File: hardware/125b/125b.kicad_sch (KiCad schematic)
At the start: 51 parts, among them J1 Guitar in, J2 Barrel_Jack, J3 Conn_02x05_Odd_Even_MountingP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, J4 Guitar out, SW1 SW_DIP_x02, SW2 RotaryEncoder_Switch, SW3 Switch 1, SW4 Switch 2, U1 L78L05_TO92, U2 TL074

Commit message: Everything connected together
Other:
- moved on the sheet: D1
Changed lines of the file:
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@@
 	(wire
 		(pts
-			(xy 26.67 153.67) (xy 30.48 153.67)
+			(xy 29.21 153.67) (xy 33.02 153.67)
 		)
 		(stroke
@@
 	(wire
 		(pts
+			(xy 19.05 153.67) (xy 21.59 153.67)
+		)
+		(stroke
+			(width 0)
+			(type default)
+		)
+	)
+	(wire
+		(pts
 			(xy 133.35 52.07) (xy 148.59 52.07)
 		)
@@
 	)
 	(label "fsw2"
-		(at 30.48 153.67 0)
+		(at 33.02 153.67 0)
 		(effects
 			(font
@@
 		)
 	)
+	(netclass_flag ""
+		(length 2.54)
+		(shape round)
+		(at 53.34 161.29 0)
+		(fields_autoplaced yes)
+		(effects
+			(font
+				(size 1.27 1.27)
+			)
+			(justify left bottom)
+		)
+		(property "Netclass" "Power"
+			(at 54.0385 158.75 0)
+			(effects
+				(font
+					(size 1.27 1.27)
+				)
+				(justify left)
+			)
+		)
+		(property "Component Class" ""
+			(at 1.27 1.27 0)
+			(effects
+				(font
+					(size 1.27 1.27)
+					(italic yes)
+				)
+			)
+		)
+	)
+	(netclass_flag ""
+		(length 2.54)
+		(shape round)
+		(at 111.76 161.29 0)
+		(fields_autoplaced yes)
+		(effects
+			(font
+				(size 1.27 1.27)
+			)
+			(justify left bottom)
+		)
+		(property "Netclass" "Power"
+			(at 112.4585 158.75 0)
+			(effects
+				(font
+					(size 1.27 1.27)
+				)
+				(justify left)
+			)
+		)
+		(property "Component Class" ""
+			(at -1.27 0 0)
+			(effects
+				(font
+					(size 1.27 1.27)
+					(italic yes)
+				)
+			)
+		)
+	)
+	(netclass_flag ""
+		(length 2.54)
+		(shape round)
+		(at 31.75 153.67 0)
+		(fields_autoplaced yes)
+		(effects
+			(font
+				(size 1.27 1.27)
+			)
+			(justify left bottom)
+		)
+		(property "Netclass" "Power"
+			(at 32.4485 151.13 0)
+			(effects
+				(font
+					(size 1.27 1.27)
+				)
+				(justify left)
+			)
+		)
+		(property "Component Class" ""
+			(at -45.72 8.89 0)
+			(effects
+				(font
+					(size 1.27 1.27)
+					(italic yes)
+				)
+			)
+		)
+	)
+	(netclass_flag ""
+		(length 2.54)
+		(shape round)
+		(at 20.32 153.67 0)
+		(fields_autoplaced yes)
+		(effects
+			(font
+				(size 1.27 1.27)
+			)
+			(justify left bottom)
+		)
+		(property "Netclass" "Power"
+			(at 21.0185 151.13 0)
+			(effects
+				(font
+					(size 1.27 1.27)
+				)
+				(justify left)
+			)
+		)
+		(property "Component Class" ""
+			(at -57.15 8.89 0)
+			(effects
+				(font
+					(size 1.27 1.27)
+					(italic yes)
+				)
+			)
+		)
+	)
+	(netclass_flag ""
+		(length 2.54)
+		(shape round)
+		(at 27.94 161.29 0)
+		(fields_autoplaced yes)
+		(effects
+			(font
+				(size 1.27 1.27)
+			)
+			(justify left bottom)
+		)
+		(property "Netclass" "Power"
+			(at 28.6385 158.75 0)
+			(effects
+				(font
+					(size 1.27 1.27)
+				)
+				(justify left)
+			)
+		)
+		(property "Component Class" ""
+			(at -168.91 17.78 0)
+			(effects
+				(font
+					(size 1.27 1.27)
+					(italic yes)
+				)
+			)
+		)
+	)
 	(symbol
 		(lib_name "GND_15")
@@
 	(symbol
 		(lib_id "Device:LED")
-		(at 22.86 153.67 180)
+		(at 25.4 153.67 180)
 		(unit 1)
 		(exclude_from_sim no)
@@
 		(on_board yes)
 		(dnp no)
-		(fields_autoplaced yes)
 		(property "Reference" "D1"
-			(at 24.4475 146.05 0)
+			(at 29.5275 146.05 0)
 			(effects
 				(font
@@
 		)
 		(property "Value" "LED"
-			(at 24.4475 148.59 0)
+			(at 29.5275 148.59 0)
 			(effects
 				(font
@@
 		)
 		(property "Footprint" "LED_THT:LED_D1.8mm_W3.3mm_H2.4mm"
-			(at 22.86 153.67 0)
+			(at 25.4 153.67 0)
 			(effects
 				(font
@@
 		)
 		(property "Datasheet" "~"
-			(at 22.86 153.67 0)
+			(at 25.4 153.67 0)
 			(effects
 				(font
@@
 		)
 		(property "Description" "Light emitting diode"
-			(at 22.86 153.67 0)
+			(at 25.4 153.67 0)
 			(effects
 				(font
@@
 		)
 		(property "Sim.Pins" "1=K 2=A"
-			(at 22.86 153.67 0)
+			(at 25.4 153.67 0)
 			(effects
 				(font

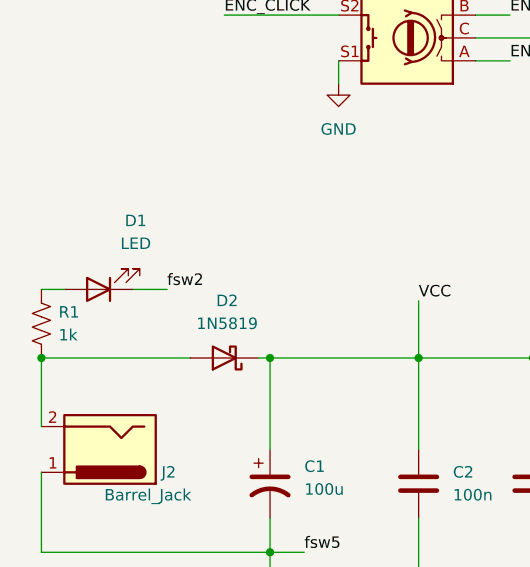
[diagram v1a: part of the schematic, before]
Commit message: Set up power nets to have wider traces
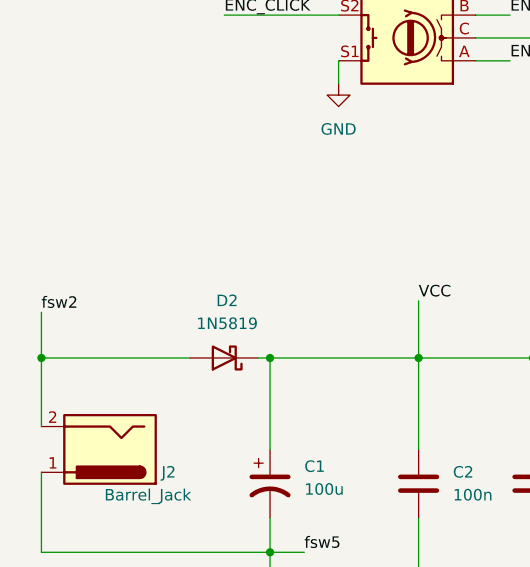
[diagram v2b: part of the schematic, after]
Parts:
- removed D1: LED, LED_THT:LED_D1.8mm_W3.3mm_H2.4mm, symbol Device:LED
- removed R1: 1k, Resistor_SMD:R_1206_3216Metric, symbol Device:R_US
- A1: footprint Library:Electrosmith_Daisy_Seed -> Project:Electrosmith_Daisy_Seed
- J1, J4: footprint Library:Jack_6.35mm_Neutrik_NRJ6HF-1-AU_Horizontal -> Project:Jack_6.35mm_Neutrik_NRJ6HF-1-AU_Horizontal
- U1: footprint Library:TO-92_Inline_Wide_78L05_dc -> Project:TO-92_Inline_Wide_78L05_dc
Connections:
- net fsw2: now also D2.2 (A), J2.2
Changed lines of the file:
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@@
 	(title_block
 		(title "Podal")
-		(date "2025-06-09")
-		(rev "0.4")
+		(date "2025-08-03")
+		(rev "0.5")
 	)
 	(text "Terminate unused op-amp"
@@
 	)
 	(junction
-		(at 264.16 33.02)
+		(at 19.05 161.29)
 		(diameter 0)
 		(color 0 0 0 0)
 	)
 	(junction
-		(at 26.67 52.07)
+		(at 264.16 33.02)
 		(diameter 0)
 		(color 0 0 0 0)
 	)
 	(junction
-		(at 19.05 161.29)
+		(at 26.67 52.07)
 		(diameter 0)
 		(color 0 0 0 0)
@@
 	(wire
 		(pts
-			(xy 29.21 153.67) (xy 33.02 153.67)
-		)
-		(stroke
-			(width 0)
-			(type default)
-		)
-	)
-	(wire
-		(pts
 			(xy 43.18 161.29) (xy 44.45 161.29)
 		)
@@
 	(wire
 		(pts
-			(xy 19.05 153.67) (xy 21.59 153.67)
-		)
-		(stroke
-			(width 0)
-			(type default)
-		)
-	)
-	(wire
-		(pts
 			(xy 133.35 52.07) (xy 148.59 52.07)
 		)
@@
 	(wire
 		(pts
+			(xy 19.05 156.21) (xy 19.05 161.29)
+		)
+		(stroke
+			(width 0)
+			(type default)
+		)
+	)
+	(wire
+		(pts
 			(xy 19.05 182.88) (xy 44.45 182.88)
 		)
@@
 	)
 	(label "fsw2"
-		(at 33.02 153.67 0)
+		(at 19.05 156.21 0)
 		(effects
 			(font
@@
 		(length 2.54)
 		(shape round)
-		(at 31.75 153.67 0)
-		(fields_autoplaced yes)
-		(effects
-			(font
-				(size 1.27 1.27)
-			)
-			(justify left bottom)
-		)
-		(property "Netclass" "Power"
-			(at 32.4485 151.13 0)
-			(effects
-				(font
-					(size 1.27 1.27)
-				)
-				(justify left)
-			)
-		)
-		(property "Component Class" ""
-			(at -45.72 8.89 0)
-			(effects
-				(font
-					(size 1.27 1.27)
-					(italic yes)
-				)
-			)
-		)
-	)
-	(netclass_flag ""
-		(length 2.54)
-		(shape round)
-		(at 20.32 153.67 0)
-		(fields_autoplaced yes)
-		(effects
-			(font
-				(size 1.27 1.27)
-			)
-			(justify left bottom)
-		)
-		(property "Netclass" "Power"
-			(at 21.0185 151.13 0)
-			(effects
-				(font
-					(size 1.27 1.27)
-				)
-				(justify left)
-			)
-		)
-		(property "Component Class" ""
-			(at -57.15 8.89 0)
-			(effects
-				(font
-					(size 1.27 1.27)
-					(italic yes)
-				)
-			)
-		)
-	)
-	(netclass_flag ""
-		(length 2.54)
-		(shape round)
 		(at 27.94 161.29 0)
 		(fields_autoplaced yes)
@@
 			)
 		)
-		(property "Footprint" "Library:Jack_6.35mm_Neutrik_NRJ6HF-1-AU_Horizontal"
+		(property "Footprint" "Project:Jack_6.35mm_Neutrik_NRJ6HF-1-AU_Horizontal"
 			(at 267.97 100.33 0)
 			(effects
@@
 			)
 		)
-		(property "Footprint" "Library:TO-92_Inline_Wide_78L05_dc"
+		(property "Footprint" "Project:TO-92_Inline_Wide_78L05_dc"
 			(at 90.17 155.575 0)
 			(effects
@@
 			)
 		)
-		(property "Footprint" "Library:Electrosmith_Daisy_Seed"
+		(property "Footprint" "Project:Electrosmith_Daisy_Seed"
 			(at 181.61 140.97 0)
 			(effects
@@
 	)
 	(symbol
-		(lib_id "Device:LED")
-		(at 25.4 153.67 180)
-		(unit 1)
-		(exclude_from_sim no)
-		(in_bom yes)
-		(on_board yes)
-		(dnp no)
-		(property "Reference" "D1"
-			(at 29.5275 146.05 0)
-			(effects
-				(font
-					(size 1.27 1.27)
-				)
-			)
-		)
-		(property "Value" "LED"
-			(at 29.5275 148.59 0)
-			(effects
-				(font
-					(size 1.27 1.27)
-				)
-			)
-		)
-		(property "Footprint" "LED_THT:LED_D1.8mm_W3.3mm_H2.4mm"
-			(at 25.4 153.67 0)
-			(effects
-				(font
-					(size 1.27 1.27)
-				)
-				(hide yes)
-			)
-		)
-		(property "Datasheet" "~"
-			(at 25.4 153.67 0)
-			(effects
-				(font
-					(size 1.27 1.27)
-				)
-				(hide yes)
-			)
-		)
-		(property "Description" "Light emitting diode"
-			(at 25.4 153.67 0)
-			(effects
-				(font
-					(size 1.27 1.27)
-				)
-				(hide yes)
-			)
-		)
-		(property "Sim.Pins" "1=K 2=A"
-			(at 25.4 153.67 0)
-			(effects
-				(font
-					(size 1.27 1.27)
-				)
-				(hide yes)
-			)
-		)
-		(pin "1"
-		)
-		(pin "2"
-		)
-		(instances
-			(project "podal_1590b"
-				(path "/12e895f7-e5ae-4934-aed6-e6e04c63dd03"
-					(reference "D1")
-					(unit 1)
-				)
-			)
-		)
-	)
-	(symbol
 		(lib_id "Switch:SW_Push_Dual")
 		(at 101.6 134.62 180)
@@
 			)
 		)
-		(property "Footprint" "Library:Jack_6.35mm_Neutrik_NRJ6HF-1-AU_Horizontal"
+		(property "Footprint" "Project:Jack_6.35mm_Neutrik_NRJ6HF-1-AU_Horizontal"
 			(at 22.86 26.67 0)
 			(effects
@@
 					(unit 1)
 				)
-			)
-		)
-	)
-	(symbol
-		(lib_id "Device:R_US")
-		(at 19.05 157.48 180)
-		(unit 1)
-		(exclude_from_sim no)
-		(in_bom yes)
-		(on_board yes)
-		(dnp no)
-		(fields_autoplaced yes)
-		(property "Reference" "R1"
-			(at 20.955 156.21 0)
-			(effects
-				(font
-					(size 1.27 1.27)
-				)
-				(justify right)
-			)
-		)
-		(property "Value" "1k"
-			(at 20.955 158.75 0)
-			(effects
-				(font
-					(size 1.27 1.27)
-				)
-				(justify right)
-			)
-		)
-		(property "Footprint" "Resistor_SMD:R_1206_3216Metric"
-			(at 18.034 157.226 90)
-			(effects
-				(font
-					(size 1.27 1.27)
-				)
-				(hide yes)
-			)
-		)
-		(property "Datasheet" "~"
-			(at 19.05 157.48 0)
-			(effects
-				(font
-					(size 1.27 1.27)
-				)
-				(hide yes)
-			)
-		)
-		(property "Description" ""
-			(at 19.05 157.48 0)
-			(effects
-				(font
-					(size 1.27 1.27)
-				)
-				(hide yes)
-			)
-		)
-		(pin "1"
-		)
-		(pin "2"
-		)
-		(instances
-			(project "podal_1590b"
-				(path "/12e895f7-e5ae-4934-aed6-e6e04c63dd03"
-					(reference "R1")
-					(unit 1)
-				)
